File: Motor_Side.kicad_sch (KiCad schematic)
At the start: 30 parts, among them U2 TLV9301xDCK, U3 TLV9301xDCK, U4 TCMT1106, U5 TCMT1106

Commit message: further schematic changes
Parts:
- renumbered Ref_TP2 to A_Ref_TP2, SigHV_TP2 to A_SigHV2, SignalLV2 to A_SignalLV2, Ref_TP1 to M_Ref_TP1, SigHV_TP1 to M_SigHV1, SignalLV1 to M_SignalLV1
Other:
- moved on the sheet: A_SignalLV2, OptVf_TP2, R15, U5
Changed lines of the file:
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@@
 	)
 	(junction
-		(at 184.15 139.7)
+		(at 181.61 139.7)
 		(diameter 0)
 		(color 0 0 0 0)
@@
 	)
 	(junction
-		(at 154.94 134.62)
+		(at 152.4 134.62)
 		(diameter 0)
 		(color 0 0 0 0)
@@
 	(wire
 		(pts
-			(xy 154.94 134.62) (xy 158.75 134.62)
+			(xy 152.4 134.62) (xy 156.21 134.62)
 		)
 		(stroke
@@
 	(wire
 		(pts
-			(xy 144.78 134.62) (xy 154.94 134.62)
+			(xy 142.24 134.62) (xy 152.4 134.62)
 		)
 		(stroke
@@
 		)
 	)
+	(polyline
+		(pts
+			(xy 163.83 13.97) (xy 163.83 195.58)
+		)
+		(stroke
+			(width 0.254)
+			(type dash)
+		)
+	)
 	(wire
 		(pts
@@
 	(wire
 		(pts
-			(xy 144.78 119.38) (xy 144.78 123.19)
+			(xy 142.24 119.38) (xy 142.24 123.19)
 		)
 		(stroke
@@
 	(wire
 		(pts
-			(xy 184.15 139.7) (xy 189.23 139.7)
+			(xy 181.61 139.7) (xy 186.69 139.7)
 		)
 		(stroke
@@
 	(wire
 		(pts
-			(xy 184.15 140.97) (xy 184.15 139.7)
+			(xy 181.61 140.97) (xy 181.61 139.7)
 		)
 		(stroke
@@
 	(wire
 		(pts
-			(xy 173.99 139.7) (xy 184.15 139.7)
+			(xy 171.45 139.7) (xy 181.61 139.7)
 		)
 		(stroke
@@
 	(wire
 		(pts
-			(xy 144.78 139.7) (xy 158.75 139.7)
+			(xy 142.24 139.7) (xy 156.21 139.7)
 		)
 		(stroke
@@
 	(wire
 		(pts
-			(xy 173.99 134.62) (xy 177.8 134.62)
+			(xy 171.45 134.62) (xy 175.26 134.62)
 		)
 		(stroke
@@
 	(wire
 		(pts
-			(xy 177.8 129.54) (xy 177.8 134.62)
+			(xy 175.26 129.54) (xy 175.26 134.62)
 		)
 		(stroke
@@
 	(wire
 		(pts
-			(xy 144.78 134.62) (xy 144.78 130.81)
+			(xy 142.24 134.62) (xy 142.24 130.81)
 		)
 		(stroke
@@
 	(text "Optocoupler\n(Galvonic isolation)"
 		(exclude_from_sim no)
-		(at 166.878 144.526 0)
+		(at 164.338 144.526 0)
 		(effects
 			(font
@@
 	)
 	(label "Arr_SignalHV"
-		(at 144.78 139.7 0)
+		(at 142.24 139.7 0)
 		(fields_autoplaced yes)
 		(effects
@@
 	(hierarchical_label "ISO_PWR"
 		(shape input)
-		(at 144.78 119.38 0)
+		(at 142.24 119.38 0)
 		(fields_autoplaced yes)
 		(effects
@@
 	(hierarchical_label "Arr_Signal"
 		(shape input)
-		(at 189.23 139.7 0)
+		(at 186.69 139.7 0)
 		(fields_autoplaced yes)
 		(effects
@@
 	(hierarchical_label "LV+"
 		(shape input)
-		(at 177.8 129.54 0)
+		(at 175.26 129.54 0)
 		(fields_autoplaced yes)
 		(effects
@@
 		(dnp no)
 		(fields_autoplaced yes)
-		(property "Reference" "Ref_TP1"
+		(property "Reference" "M_Ref_TP1"
 			(at 81.28 39.3699 90)
 			(effects
@@
 			(project "ActivePrecharge"
 				(path "/b9847a31-2b3b-47ca-9561-fab506416f6d/27dbb16c-0867-45c1-9eb8-11b8a424e215"
-					(reference "Ref_TP1")
+					(reference "M_Ref_TP1")
 					(unit 1)
 				)
@@
 		(dnp no)
 		(fields_autoplaced yes)
-		(property "Reference" "Ref_TP2"
+		(property "Reference" "A_Ref_TP2"
 			(at 83.82 121.9199 90)
 			(effects
@@
 			(project "ActivePrecharge"
 				(path "/b9847a31-2b3b-47ca-9561-fab506416f6d/27dbb16c-0867-45c1-9eb8-11b8a424e215"
-					(reference "Ref_TP2")
+					(reference "A_Ref_TP2")
 					(unit 1)
 				)
@@
 	(symbol
 		(lib_id "Connector:TestPoint")
-		(at 184.15 140.97 180)
+		(at 181.61 140.97 180)
 		(unit 1)
 		(exclude_from_sim no)
@@
 		(dnp no)
 		(fields_autoplaced yes)
-		(property "Reference" "SignalLV2"
-			(at 186.69 143.0019 0)
+		(property "Reference" "A_SignalLV2"
+			(at 184.15 143.0019 0)
 			(effects
 				(font
@@
 		)
 		(property "Value" "TestPoint"
-			(at 186.69 145.5419 0)
+			(at 184.15 145.5419 0)
 			(effects
 				(font
@@
 		)
 		(property "Footprint" "utsvt-special:TestPoint_HEX_3mmID"
-			(at 179.07 140.97 0)
+			(at 176.53 140.97 0)
 			(effects
 				(font
@@
 		)
 		(property "Datasheet" "~"
-			(at 179.07 140.97 0)
+			(at 176.53 140.97 0)
 			(effects
 				(font
@@
 		)
 		(property "Description" "test point"
-			(at 184.15 140.97 0)
+			(at 181.61 140.97 0)
 			(effects
 				(font
@@
 			(project "ActivePrecharge"
 				(path "/b9847a31-2b3b-47ca-9561-fab506416f6d/27dbb16c-0867-45c1-9eb8-11b8a424e215"
-					(reference "SignalLV2")
+					(reference "A_SignalLV2")
 					(unit 1)
 				)
@@
 		(dnp no)
 		(fields_autoplaced yes)
-		(property "Reference" "SignalLV1"
+		(property "Reference" "M_SignalLV1"
 			(at 184.15 60.4519 0)
 			(effects
@@
 			(project "ActivePrecharge"
 				(path "/b9847a31-2b3b-47ca-9561-fab506416f6d/27dbb16c-0867-45c1-9eb8-11b8a424e215"
-					(reference "SignalLV1")
+					(reference "M_SignalLV1")
 					(unit 1)
 				)
@@
 	(symbol
 		(lib_id "Device:R_US")
-		(at 144.78 127 180)
+		(at 142.24 127 180)
 		(unit 1)
 		(exclude_from_sim no)
@@
 		(fields_autoplaced yes)
 		(property "Reference" "R15"
-			(at 147.32 125.7299 0)
+			(at 144.78 125.7299 0)
 			(effects
 				(font
@@
 		)
 		(property "Value" "380"
-			(at 147.32 128.2699 0)
+			(at 144.78 128.2699 0)
 			(effects
 				(font
@@
 		)
 		(property "Footprint" "Resistor_SMD:R_0805_2012Metric"
-			(at 143.764 126.746 90)
+			(at 141.224 126.746 90)
 			(effects
 				(font
@@
 		)
 		(property "Datasheet" "~"
-			(at 144.78 127 0)
+			(at 142.24 127 0)
 			(effects
 				(font
@@
 		)
 		(property "Description" "Resistor, US symbol"
-			(at 144.78 127 0)
+			(at 142.24 127 0)
 			(effects
 				(font
@@
 		(on_board yes)
 		(dnp no)
-		(property "Reference" "SigHV_TP1"
+		(property "Reference" "M_SigHV1"
 			(at 96.52 52.324 0)
 			(effects
@@
 			(project "ActivePrecharge"
 				(path "/b9847a31-2b3b-47ca-9561-fab506416f6d/27dbb16c-0867-45c1-9eb8-11b8a424e215"
-					(reference "SigHV_TP1")
+					(reference "M_SigHV1")
 					(unit 1)
 				)
@@
 	(symbol
 		(lib_id "Connector:TestPoint")
-		(at 154.94 134.62 0)
+		(at 152.4 134.62 0)
 		(unit 1)
 		(exclude_from_sim no)
@@
 		(dnp no)
 		(property "Reference" "OptVf_TP2"
-			(at 161.544 128.524 0)
+			(at 159.004 128.524 0)
 			(effects
 				(font
@@
 		)
 		(property "Value" "TestPoint"
-			(at 160.782 125.984 0)
+			(at 158.242 125.984 0)
 			(effects
 				(font
@@
 		)
 		(property "Footprint" "utsvt-special:TestPoint_HEX_3mmID"
-			(at 160.02 134.62 0)
+			(at 157.48 134.62 0)
 			(effects
 				(font
@@
 		)
 		(property "Datasheet" "~"
-			(at 160.02 134.62 0)
+			(at 157.48 134.62 0)
 			(effects
 				(font
@@
 		)
 		(property "Description" "test point"
-			(at 154.94 134.62 0)
+			(at 152.4 134.62 0)
 			(effects
 				(font
@@
 	(symbol
 		(lib_id "Isolator:TCMT1106")
-		(at 166.37 137.16 0)
+		(at 163.83 137.16 0)
 		(unit 1)
 		(exclude_from_sim no)
@@
 		(fields_autoplaced yes)
 		(property "Reference" "U5"
-			(at 166.37 128.27 0)
+			(at 163.83 128.27 0)
 			(effects
 				(font
@@
 		)
 		(property "Value" "TCMT1106"
-			(at 166.37 130.81 0)
+			(at 163.83 130.81 0)
 			(effects
 				(font
@@
 		)
 		(property "Footprint" "Package_SO:SOP-4_4.4x2.6mm_P1.27mm"
-			(at 166.37 144.78 0)
+			(at 163.83 144.78 0)
 			(effects
 				(font
@@
 		)
 		(property "Datasheet" "https://www.vishay.com/docs/83510/tcmt11.pdf"
-			(at 166.37 138.43 0)
+			(at 163.83 138.43 0)
 			(effects
 				(font
@@
 		)
 		(property "Description" "Optocoupler, Vce 70V, CTR 100-300%, Viso 3750V (RMS), SOP-4"
-			(at 166.37 137.16 0)
+			(at 163.83 137.16 0)
 			(effects
 				(font
@@
 		(on_board yes)
 		(dnp no)
-		(property "Reference" "SigHV_TP2"
+		(property "Reference" "A_SigHV2"
 			(at 99.06 134.874 0)
 			(effects
@@
 			(project "ActivePrecharge"
 				(path "/b9847a31-2b3b-47ca-9561-fab506416f6d/27dbb16c-0867-45c1-9eb8-11b8a424e215"
-					(reference "SigHV_TP2")
+					(reference "A_SigHV2")
 					(unit 1)
 				)

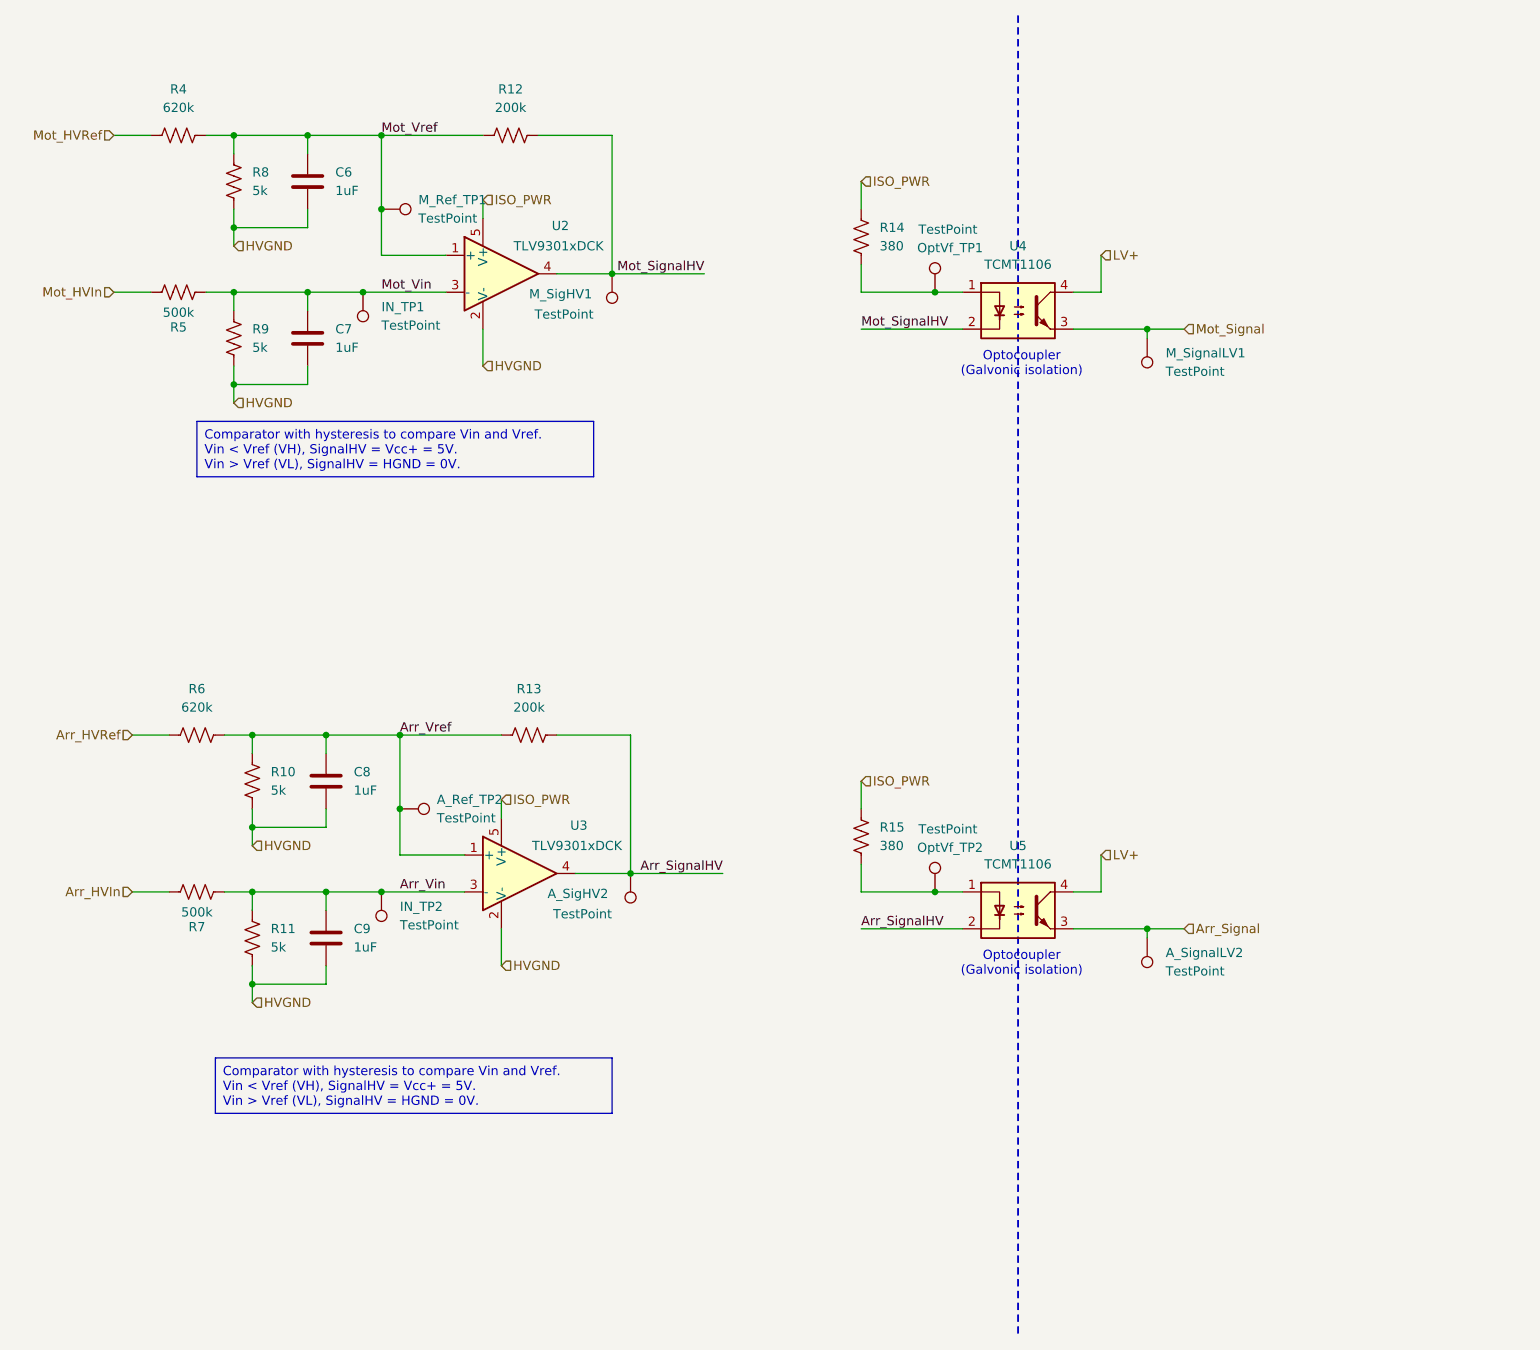
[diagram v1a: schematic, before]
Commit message: fixed some ERC errors, incorrect connectors
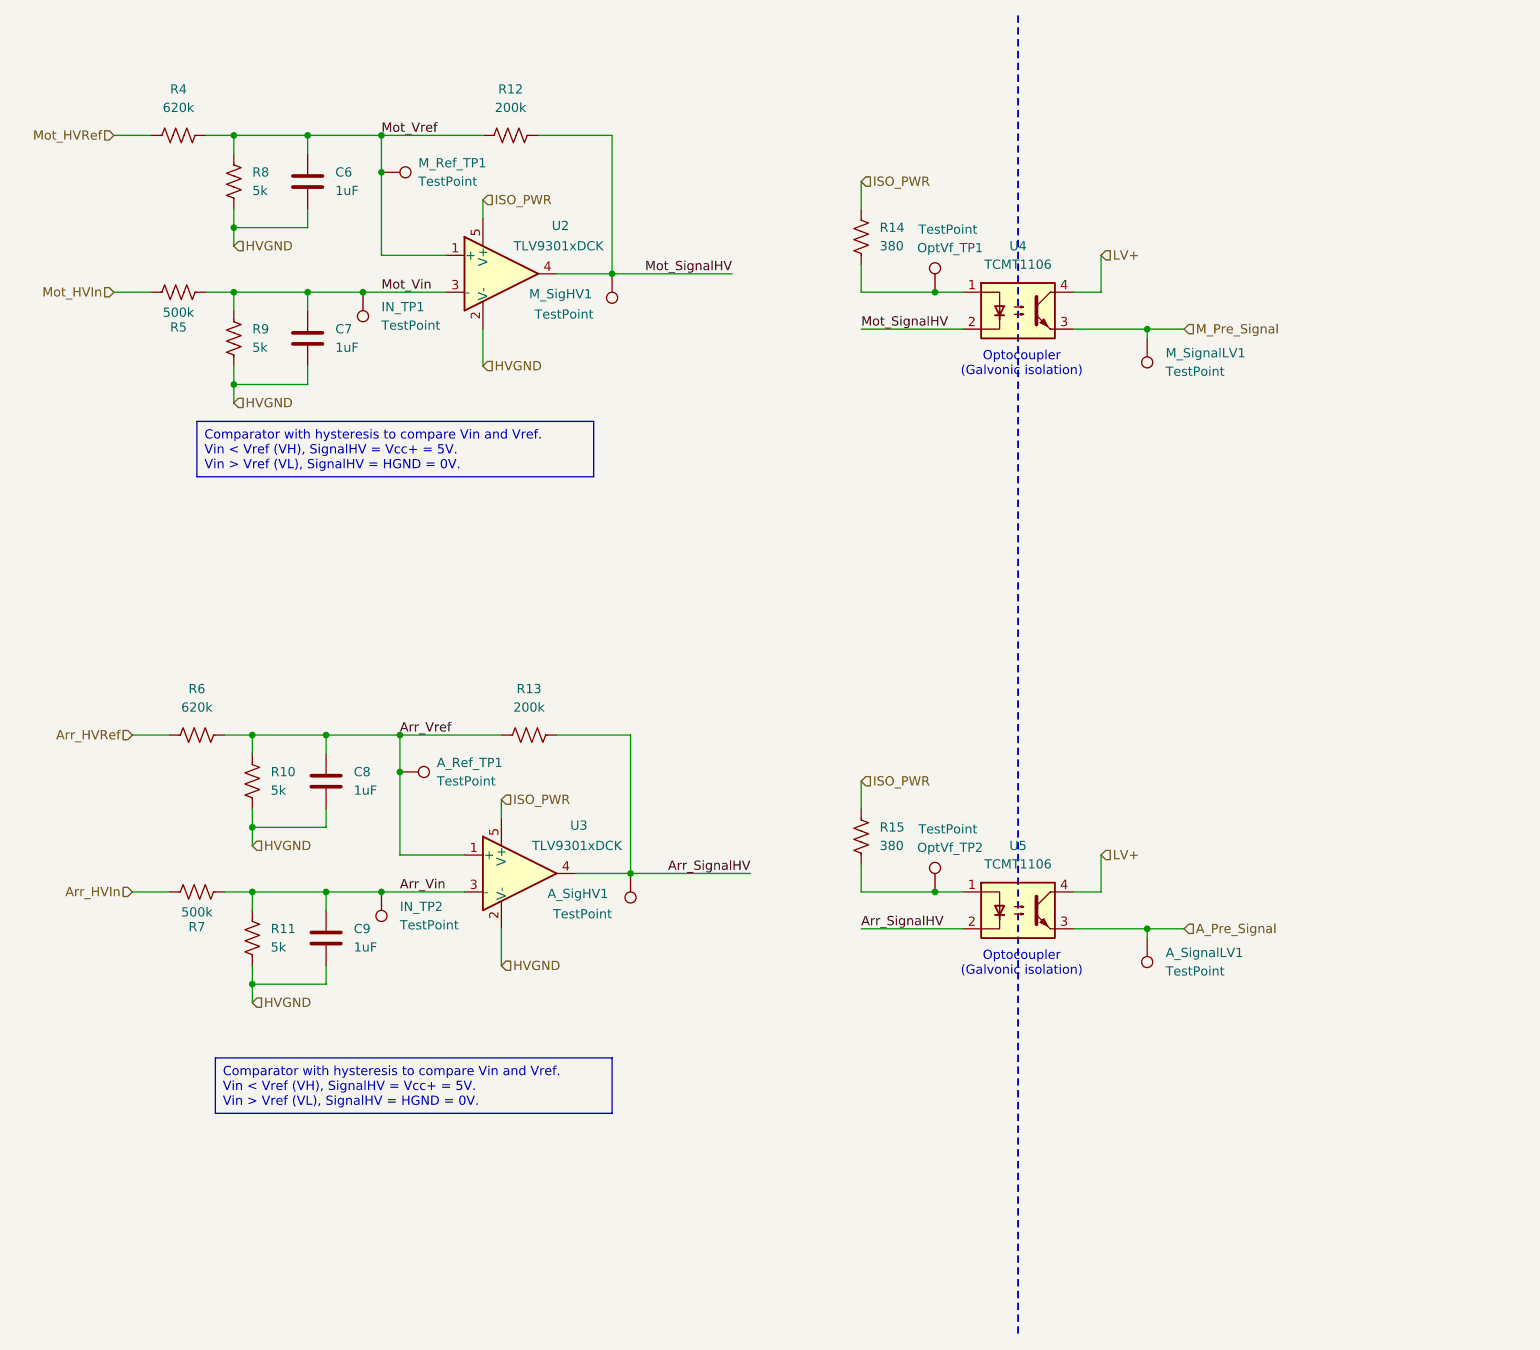
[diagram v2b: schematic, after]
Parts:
- renumbered A_Ref_TP2 to A_Ref_TP1, A_SigHV2 to A_SigHV1, A_SignalLV2 to A_SignalLV1
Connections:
- net Arr_Signal renamed A_Pre_Signal
- net Mot_Signal renamed M_Pre_Signal
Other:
- moved on the sheet: A_Ref_TP1, M_Ref_TP1
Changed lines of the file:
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@@
-	)
-	(junction
-		(at 76.2 40.64)
-		(diameter 0)
-		(color 0 0 0 0)
 	)
 	(junction
@@
 	)
 	(junction
+		(at 76.2 35.56)
+		(diameter 0)
+		(color 0 0 0 0)
+	)
+	(junction
 		(at 76.2 30.48)
 		(diameter 0)
@@
 	)
 	(junction
-		(at 68.58 113.03)
+		(at 78.74 118.11)
 		(diameter 0)
 		(color 0 0 0 0)
 	)
 	(junction
-		(at 78.74 123.19)
+		(at 68.58 113.03)
 		(diameter 0)
 		(color 0 0 0 0)
@@
 	(wire
 		(pts
-			(xy 76.2 30.48) (xy 76.2 40.64)
+			(xy 76.2 30.48) (xy 76.2 35.56)
 		)
 		(stroke
@@
 		(pts
 			(xy 90.17 62.23) (xy 90.17 57.15)
+		)
+		(stroke
+			(width 0)
+			(type default)
+		)
+	)
+	(wire
+		(pts
+			(xy 78.74 118.11) (xy 78.74 129.54)
 		)
 		(stroke
@@
 	(wire
 		(pts
-			(xy 107.95 49.53) (xy 120.65 49.53)
+			(xy 107.95 49.53) (xy 124.46 49.53)
 		)
 		(stroke
@@
 	(wire
 		(pts
+			(xy 76.2 35.56) (xy 76.2 46.99)
+		)
+		(stroke
+			(width 0)
+			(type default)
+		)
+	)
+	(wire
+		(pts
 			(xy 142.24 119.38) (xy 142.24 123.19)
 		)
@@
 	(wire
 		(pts
-			(xy 76.2 40.64) (xy 76.2 46.99)
-		)
-		(stroke
-			(width 0)
-			(type default)
-		)
-	)
-	(wire
-		(pts
 			(xy 85.09 52.07) (xy 73.66 52.07)
 		)
@@
 	(wire
 		(pts
-			(xy 110.49 132.08) (xy 123.19 132.08)
+			(xy 110.49 132.08) (xy 127 132.08)
 		)
 		(stroke
@@
 	(wire
 		(pts
-			(xy 78.74 123.19) (xy 78.74 129.54)
-		)
-		(stroke
-			(width 0)
-			(type default)
-		)
-	)
-	(wire
-		(pts
 			(xy 66.04 64.77) (xy 55.88 64.77)
 		)
@@
 	(wire
 		(pts
-			(xy 78.74 113.03) (xy 78.74 123.19)
+			(xy 78.74 113.03) (xy 78.74 118.11)
 		)
 		(stroke
@@
 	)
 	(label "Mot_SignalHV"
-		(at 120.65 49.53 180)
+		(at 124.46 49.53 180)
 		(fields_autoplaced yes)
 		(effects
@@
 	)
 	(label "Arr_SignalHV"
-		(at 123.19 132.08 180)
+		(at 127 132.08 180)
 		(fields_autoplaced yes)
 		(effects
@@
 		)
 	)
-	(hierarchical_label "Mot_Signal"
+	(hierarchical_label "M_Pre_Signal"
 		(shape input)
 		(at 186.69 57.15 0)
@@
 		)
 	)
-	(hierarchical_label "Arr_Signal"
+	(hierarchical_label "A_Pre_Signal"
 		(shape input)
 		(at 186.69 139.7 0)
@@
 	(symbol
 		(lib_id "Connector:TestPoint")
-		(at 76.2 40.64 270)
+		(at 76.2 35.56 270)
 		(unit 1)
 		(exclude_from_sim no)
@@
 		(fields_autoplaced yes)
 		(property "Reference" "M_Ref_TP1"
-			(at 81.28 39.3699 90)
+			(at 81.28 34.2899 90)
 			(effects
 				(font
@@
 		)
 		(property "Value" "TestPoint"
-			(at 81.28 41.9099 90)
+			(at 81.28 36.8299 90)
 			(effects
 				(font
@@
 		)
 		(property "Footprint" "utsvt-special:TestPoint_HEX_3mmID"
-			(at 76.2 45.72 0)
+			(at 76.2 40.64 0)
 			(effects
 				(font
@@
 		)
 		(property "Datasheet" "~"
-			(at 76.2 45.72 0)
+			(at 76.2 40.64 0)
 			(effects
 				(font
@@
 		)
 		(property "Description" "test point"
-			(at 76.2 40.64 0)
+			(at 76.2 35.56 0)
 			(effects
 				(font
@@
 	(symbol
 		(lib_id "Connector:TestPoint")
-		(at 78.74 123.19 270)
+		(at 78.74 118.11 270)
 		(unit 1)
 		(exclude_from_sim no)
@@
 		(dnp no)
 		(fields_autoplaced yes)
-		(property "Reference" "A_Ref_TP2"
-			(at 83.82 121.9199 90)
+		(property "Reference" "A_Ref_TP1"
+			(at 83.82 116.8399 90)
 			(effects
 				(font
@@
 		)
 		(property "Value" "TestPoint"
-			(at 83.82 124.4599 90)
+			(at 83.82 119.3799 90)
 			(effects
 				(font
@@
 		)
 		(property "Footprint" "utsvt-special:TestPoint_HEX_3mmID"
-			(at 78.74 128.27 0)
+			(at 78.74 123.19 0)
 			(effects
 				(font
@@
 		)
 		(property "Datasheet" "~"
-			(at 78.74 128.27 0)
+			(at 78.74 123.19 0)
 			(effects
 				(font
@@
 		)
 		(property "Description" "test point"
-			(at 78.74 123.19 0)
+			(at 78.74 118.11 0)
 			(effects
 				(font
@@
 			(project "ActivePrecharge"
 				(path "/b9847a31-2b3b-47ca-9561-fab506416f6d/27dbb16c-0867-45c1-9eb8-11b8a424e215"
-					(reference "A_Ref_TP2")
+					(reference "A_Ref_TP1")
 					(unit 1)
 				)
@@
 		(dnp no)
 		(fields_autoplaced yes)
-		(property "Reference" "A_SignalLV2"
+		(property "Reference" "A_SignalLV1"
 			(at 184.15 143.0019 0)
 			(effects
@@
 			(project "ActivePrecharge"
 				(path "/b9847a31-2b3b-47ca-9561-fab506416f6d/27dbb16c-0867-45c1-9eb8-11b8a424e215"
-					(reference "A_SignalLV2")
+					(reference "A_SignalLV1")
 					(unit 1)
 				)
@@
 		(on_board yes)
 		(dnp no)
-		(property "Reference" "A_SigHV2"
+		(property "Reference" "A_SigHV1"
 			(at 99.06 134.874 0)
 			(effects
@@
 			(project "ActivePrecharge"
 				(path "/b9847a31-2b3b-47ca-9561-fab506416f6d/27dbb16c-0867-45c1-9eb8-11b8a424e215"
-					(reference "A_SigHV2")
+					(reference "A_SigHV1")
 					(unit 1)
 				)
